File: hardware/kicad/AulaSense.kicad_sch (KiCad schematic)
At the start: 31 parts, among them J1 ESP32_DevKitV1_Header_Left, J2 ESP32_DevKitV1_Header_Right, J3 Entrada 5V, J4 Buzzer 5V, J5 DHT22, J6 PIR HC-SR501, J7 Reed switch, J8 OLED 0.96 I2C, J9 MQ-135, Q1 BC337, SW1 SW_Push, SW2 SW_Push, SW3 SW_Push

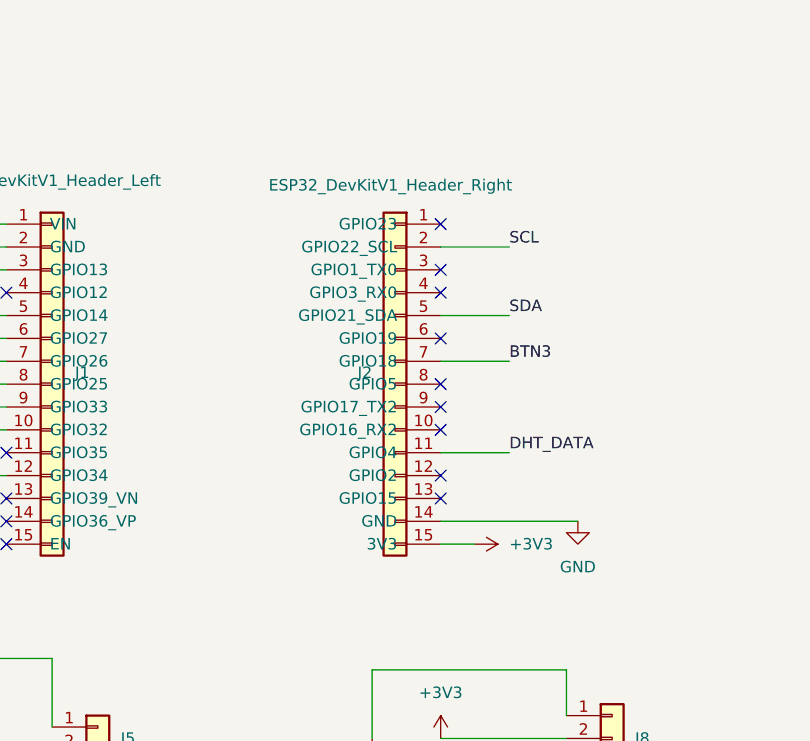
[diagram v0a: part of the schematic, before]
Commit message: feat(hw): esquematico completo, huellas THT, BOM y plano
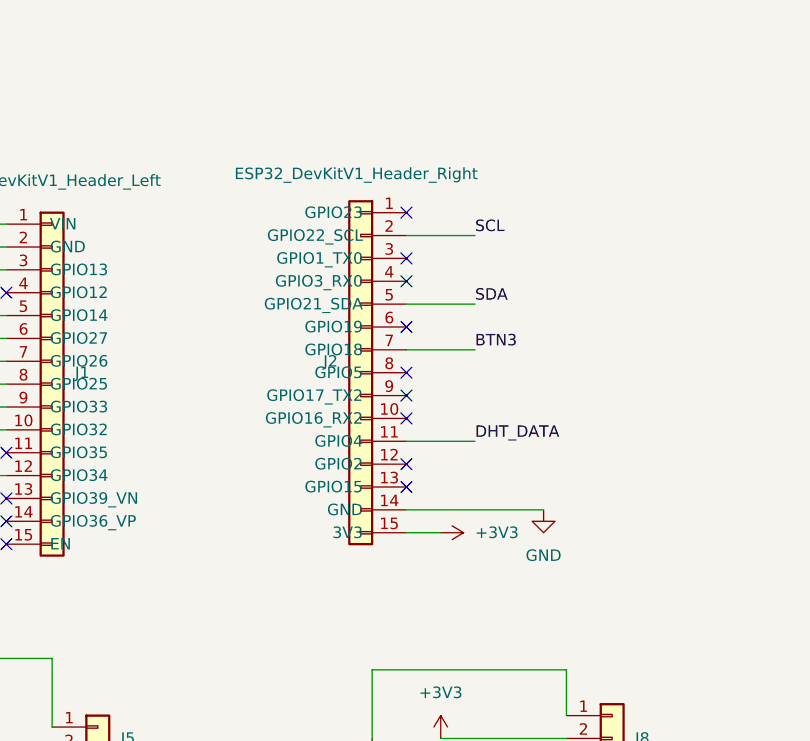
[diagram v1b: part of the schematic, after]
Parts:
- C1, C3, C4, C5, C6: footprint (none) -> Capacitor_THT:C_Disc_D5.0mm_W2.5mm_P5.00mm
- C2: footprint (none) -> Capacitor_THT:CP_Radial_D8.0mm_P3.50mm
- D1: footprint (none) -> Diode_THT:D_DO-41_SOD81_P10.16mm_Horizontal
- D2, D3, D4: footprint (none) -> LED_THT:LED_D5.0mm
- F1: footprint (none) -> Resistor_THT:R_Axial_DIN0207_L6.3mm_D2.5mm_P7.62mm_Horizontal
- J1, J2: footprint (none) -> Connector_PinSocket_2.54mm:PinSocket_1x15_P2.54mm_Vertical
- J3, J4, J7: footprint (none) -> Connector_PinHeader_2.54mm:PinHeader_1x02_P2.54mm_Vertical
- J5, J6: footprint (none) -> Connector_PinHeader_2.54mm:PinHeader_1x03_P2.54mm_Vertical
- J8, J9: footprint (none) -> Connector_PinHeader_2.54mm:PinHeader_1x04_P2.54mm_Vertical
- Q1: footprint (none) -> Package_TO_SOT_THT:TO-92_Inline
- R1, R2, R3, R4, R5, R6, R7: footprint (none) -> Resistor_THT:R_Axial_DIN0207_L6.3mm_D2.5mm_P10.16mm_Horizontal
- SW1, SW2, SW3: footprint (none) -> Button_Switch_THT:SW_PUSH_6mm
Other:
- moved on the sheet: J2
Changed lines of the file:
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@@
 	)
 	(no_connect
-		(at 166.37 83.82)
+		(at 162.56 82.55)
 	)
 	(no_connect
@@
 	)
 	(no_connect
-		(at 166.37 91.44)
+		(at 162.56 90.17)
 	)
 	(no_connect
-		(at 166.37 73.66)
+		(at 162.56 72.39)
 	)
 	(no_connect
-		(at 166.37 60.96)
+		(at 162.56 59.69)
 	)
 	(no_connect
-		(at 166.37 81.28)
+		(at 162.56 80.01)
 	)
 	(no_connect
@@
 	)
 	(no_connect
-		(at 166.37 88.9)
+		(at 162.56 87.63)
 	)
 	(no_connect
-		(at 166.37 68.58)
+		(at 162.56 67.31)
 	)
 	(no_connect
-		(at 166.37 66.04)
+		(at 162.56 64.77)
 	)
 	(no_connect
-		(at 166.37 78.74)
+		(at 162.56 77.47)
 	)
 	(no_connect
@@
 	(wire
 		(pts
-			(xy 166.37 86.36) (xy 173.99 86.36)
+			(xy 162.56 85.09) (xy 170.18 85.09)
 		)
 		(stroke
@@
 	(wire
 		(pts
-			(xy 166.37 63.5) (xy 173.99 63.5)
+			(xy 162.56 62.23) (xy 170.18 62.23)
 		)
 		(stroke
@@
 	(wire
 		(pts
-			(xy 166.37 71.12) (xy 173.99 71.12)
+			(xy 162.56 69.85) (xy 170.18 69.85)
 		)
 		(stroke
@@
 	(wire
 		(pts
-			(xy 166.37 76.2) (xy 173.99 76.2)
+			(xy 162.56 74.93) (xy 170.18 74.93)
 		)
 		(stroke
@@
 	(wire
 		(pts
-			(xy 166.37 93.98) (xy 181.61 93.98)
+			(xy 162.56 92.71) (xy 177.8 92.71)
 		)
 		(stroke
@@
 	(wire
 		(pts
-			(xy 166.37 96.52) (xy 170.18 96.52)
+			(xy 162.56 95.25) (xy 166.37 95.25)
 		)
 		(stroke
@@
 	)
 	(label "DHT_DATA"
-		(at 173.99 86.36 0)
+		(at 170.18 85.09 0)
 		(effects
 			(font
@@
 	)
 	(label "SCL"
-		(at 173.99 63.5 0)
+		(at 170.18 62.23 0)
 		(effects
 			(font
@@
 	)
 	(label "BTN3"
-		(at 173.99 76.2 0)
+		(at 170.18 74.93 0)
 		(effects
 			(font
@@
 	)
 	(label "SDA"
-		(at 173.99 71.12 0)
+		(at 170.18 69.85 0)
 		(effects
 			(font
@@
 			)
 		)
-		(property "Footprint" ""
+		(property "Footprint" "Button_Switch_THT:SW_PUSH_6mm"
 			(at 39.37 80.01 0)
 			(hide yes)
@@
 			)
 		)
-		(property "Footprint" ""
+		(property "Footprint" "Connector_PinHeader_2.54mm:PinHeader_1x04_P2.54mm_Vertical"
 			(at 185.42 118.11 0)
 			(hide yes)
@@
 			)
 		)
-		(property "Footprint" ""
+		(property "Footprint" "Capacitor_THT:CP_Radial_D8.0mm_P3.50mm"
 			(at 36.5252 52.07 0)
 			(hide yes)
@@
 			)
 		)
-		(property "Footprint" ""
+		(property "Footprint" "LED_THT:LED_D5.0mm"
 			(at 62.23 40.64 0)
 			(hide yes)
@@
 			)
 		)
-		(property "Footprint" ""
+		(property "Footprint" "Connector_PinHeader_2.54mm:PinHeader_1x03_P2.54mm_Vertical"
 			(at 128.27 134.62 0)
 			(hide yes)
@@
 			)
 		)
-		(property "Footprint" ""
+		(property "Footprint" "LED_THT:LED_D5.0mm"
 			(at 50.8 167.64 0)
 			(hide yes)
@@
 			)
 		)
-		(property "Footprint" ""
+		(property "Footprint" "Capacitor_THT:C_Disc_D5.0mm_W2.5mm_P5.00mm"
 			(at 32.7152 95.25 0)
 			(hide yes)
@@
 			)
 		)
-		(property "Footprint" ""
+		(property "Footprint" "Connector_PinHeader_2.54mm:PinHeader_1x02_P2.54mm_Vertical"
 			(at 20.32 22.86 0)
 			(hide yes)
@@
 			)
 		)
-		(property "Footprint" ""
+		(property "Footprint" "Resistor_THT:R_Axial_DIN0207_L6.3mm_D2.5mm_P10.16mm_Horizontal"
 			(at 64.77 181.102 90)
 			(hide yes)
@@
 			)
 		)
-		(property "Footprint" ""
+		(property "Footprint" "Resistor_THT:R_Axial_DIN0207_L6.3mm_D2.5mm_P10.16mm_Horizontal"
 			(at 64.77 165.862 90)
 			(hide yes)
@@
 			)
 		)
-		(property "Footprint" ""
+		(property "Footprint" "Resistor_THT:R_Axial_DIN0207_L6.3mm_D2.5mm_P10.16mm_Horizontal"
 			(at 211.582 137.16 90)
 			(hide yes)
@@
 	(symbol
 		(lib_id "AulaSense:ESP32_DevKitV1_Header_Right")
-		(at 161.29 78.74 0)
+		(at 157.48 77.47 0)
 		(mirror y)
 		(unit 1)
@@
 		(dnp no)
 		(property "Reference" "J2"
-			(at 158.75 77.4699 0)
+			(at 154.94 76.1999 0)
 			(show_name no)
 			(do_not_autoplace no)
@@
 		)
 		(property "Value" "ESP32_DevKitV1_Header_Right"
-			(at 160.782 56.642 0)
+			(at 156.972 55.372 0)
 			(show_name no)
 			(do_not_autoplace no)
@@
 			)
 		)
-		(property "Footprint" ""
-			(at 161.29 78.74 0)
+		(property "Footprint" "Connector_PinSocket_2.54mm:PinSocket_1x15_P2.54mm_Vertical"
+			(at 157.48 77.47 0)
 			(hide yes)
 			(show_name no)
@@
 		)
 		(property "Datasheet" ""
-			(at 161.29 78.74 0)
+			(at 157.48 77.47 0)
 			(hide yes)
 			(show_name no)
@@
 		)
 		(property "Description" "Generic connector, single row, 01x15, script generated (kicad-library-utils/schlib/autogen/connector/)"
-			(at 161.29 78.74 0)
+			(at 157.48 77.47 0)
 			(hide yes)
 			(show_name no)
@@
 			)
 		)
-		(property "Footprint" ""
+		(property "Footprint" "Resistor_THT:R_Axial_DIN0207_L6.3mm_D2.5mm_P10.16mm_Horizontal"
 			(at 226.822 121.92 90)
 			(hide yes)
@@
 			)
 		)
-		(property "Footprint" ""
+		(property "Footprint" "Connector_PinHeader_2.54mm:PinHeader_1x02_P2.54mm_Vertical"
 			(at 38.1 140.97 0)
 			(hide yes)
@@
 			)
 		)
-		(property "Footprint" ""
+		(property "Footprint" "Connector_PinHeader_2.54mm:PinHeader_1x03_P2.54mm_Vertical"
 			(at 128.27 119.38 0)
 			(hide yes)
@@
 			)
 		)
-		(property "Footprint" ""
+		(property "Footprint" "LED_THT:LED_D5.0mm"
 			(at 49.53 182.88 0)
 			(hide yes)
@@
 			)
 		)
-		(property "Footprint" ""
+		(property "Footprint" "Capacitor_THT:C_Disc_D5.0mm_W2.5mm_P5.00mm"
 			(at 244.8052 140.97 0)
 			(hide yes)
@@
 			)
 		)
-		(property "Footprint" ""
+		(property "Footprint" "Resistor_THT:R_Axial_DIN0207_L6.3mm_D2.5mm_P7.62mm_Horizontal"
 			(at 38.1 21.59 0)
 			(hide yes)
@@
 			)
 		)
-		(property "Footprint" ""
+		(property "Footprint" "Capacitor_THT:C_Disc_D5.0mm_W2.5mm_P5.00mm"
 			(at 32.7152 120.65 0)
 			(hide yes)
@@
 			)
 		)
-		(property "Footprint" ""
+		(property "Footprint" "Capacitor_THT:C_Disc_D5.0mm_W2.5mm_P5.00mm"
 			(at 64.4652 97.79 0)
 			(hide yes)
@@
 			)
 		)
-		(property "Footprint" ""
+		(property "Footprint" "Capacitor_THT:C_Disc_D5.0mm_W2.5mm_P5.00mm"
 			(at 36.5252 62.23 0)
 			(hide yes)
@@
 			)
 		)
-		(property "Footprint" ""
+		(property "Footprint" "Resistor_THT:R_Axial_DIN0207_L6.3mm_D2.5mm_P10.16mm_Horizontal"
 			(at 68.072 55.88 90)
 			(hide yes)
@@
 			)
 		)
-		(property "Footprint" ""
+		(property "Footprint" "Diode_THT:D_DO-41_SOD81_P10.16mm_Horizontal"
 			(at 44.45 22.86 0)
 			(hide yes)
@@
 			)
 		)
-		(property "Footprint" ""
+		(property "Footprint" "Resistor_THT:R_Axial_DIN0207_L6.3mm_D2.5mm_P10.16mm_Horizontal"
 			(at 106.172 114.3 90)
 			(hide yes)
@@
 			)
 		)
-		(property "Footprint" ""
+		(property "Footprint" "Connector_PinHeader_2.54mm:PinHeader_1x04_P2.54mm_Vertical"
 			(at 241.3 107.95 0)
 			(hide yes)
@@
 	(symbol
 		(lib_id "power:+3V3")
-		(at 170.18 96.52 270)
+		(at 166.37 95.25 270)
 		(unit 1)
 		(body_style 1)
@@
 		(fields_autoplaced yes)
 		(property "Reference" "#PWR04"
-			(at 166.37 96.52 0)
+			(at 162.56 95.25 0)
 			(hide yes)
 			(show_name no)
@@
 		)
 		(property "Value" "+3V3"
-			(at 173.99 96.5199 90)
+			(at 170.18 95.2499 90)
 			(show_name no)
 			(do_not_autoplace no)
@@
 		)
 		(property "Footprint" ""
-			(at 170.18 96.52 0)
+			(at 166.37 95.25 0)
 			(hide yes)
 			(show_name no)
@@
 		)
 		(property "Datasheet" ""
-			(at 170.18 96.52 0)
+			(at 166.37 95.25 0)
 			(hide yes)
 			(show_name no)
@@
 		)
 		(property "Description" "Power symbol creates a global label with name \"+3V3\""
-			(at 170.18 96.52 0)
+			(at 166.37 95.25 0)
 			(hide yes)
 			(show_name no)
@@
 	(symbol
 		(lib_id "power:GND")
-		(at 181.61 93.98 0)
+		(at 177.8 92.71 0)
 		(unit 1)
 		(body_style 1)
@@
 		(fields_autoplaced yes)
 		(property "Reference" "#PWR03"
-			(at 181.61 100.33 0)
+			(at 177.8 99.06 0)
 			(hide yes)
 			(show_name no)
@@
 		)
 		(property "Value" "GND"
-			(at 181.61 99.06 0)
+			(at 177.8 97.79 0)
 			(show_name no)
 			(do_not_autoplace no)
@@
 		)
 		(property "Footprint" ""
-			(at 181.61 93.98 0)
+			(at 177.8 92.71 0)
 			(hide yes)
 			(show_name no)
@@
 		)
 		(property "Datasheet" ""
-			(at 181.61 93.98 0)
+			(at 177.8 92.71 0)
 			(hide yes)
 			(show_name no)
@@
 		)
 		(property "Description" "Power symbol creates a global label with name \"GND\" , ground"
-			(at 181.61 93.98 0)
+			(at 177.8 92.71 0)
 			(hide yes)
 			(show_name no)
@@
 			)
 		)
-		(property "Footprint" ""
+		(property "Footprint" "Resistor_THT:R_Axial_DIN0207_L6.3mm_D2.5mm_P10.16mm_Horizontal"
 			(at 53.34 153.162 90)
 			(hide yes)
@@
 			)
 		)
-		(property "Footprint" ""
+		(property "Footprint" "Button_Switch_THT:SW_PUSH_6mm"
 			(at 39.37 104.14 0)
 			(hide yes)
@@
 			)
 		)
-		(property "Footprint" ""
+		(property "Footprint" "Button_Switch_THT:SW_PUSH_6mm"
 			(at 69.85 80.01 0)
 			(hide yes)
@@
 			)
 		)
-		(property "Footprint" ""
+		(property "Footprint" "Connector_PinHeader_2.54mm:PinHeader_1x02_P2.54mm_Vertical"
 			(at 128.27 153.67 0)
 			(hide yes)
@@
 			)
 		)
-		(property "Footprint" ""
+		(property "Footprint" "Connector_PinSocket_2.54mm:PinSocket_1x15_P2.54mm_Vertical"
 			(at 123.19 78.74 0)
 			(hide yes)
@@
 			)
 		)
-		(property "Footprint" ""
+		(property "Footprint" "Package_TO_SOT_THT:TO-92_Inline"
 			(at 63.5 144.78 0)
 			(hide yes)

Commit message: fix(hw): D1 a 1N5819 THT y huella radial provisional para F1
- D1: el SS34 solo existe en encapsulado SMA, se reemplaza por 1N5819 en DO-41
- F1: MF-RG300 como huella provisional, paso 5,08 mm compatible con RXEF110
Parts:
- D1: value SS34 -> 1N5819
- F1: footprint Resistor_THT:R_Axial_DIN0207_L6.3mm_D2.5mm_P7.62mm_Horizontal -> Fuse:Fuse_Bourns_MF-RG300
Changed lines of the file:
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@@
 			)
 		)
-		(property "Footprint" "Resistor_THT:R_Axial_DIN0207_L6.3mm_D2.5mm_P7.62mm_Horizontal"
+		(property "Footprint" "Fuse:Fuse_Bourns_MF-RG300"
 			(at 38.1 21.59 0)
 			(hide yes)
@@
 			)
 		)
-		(property "Value" "SS34"
+		(property "Value" "1N5819"
 			(at 44.7675 19.05 0)
 			(show_name no)
